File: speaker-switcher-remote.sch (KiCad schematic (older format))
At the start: 17 parts, among them M1 arduino-nano, Q1 TIP31C, Q2 TIP31C

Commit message: Updated with arduino src code
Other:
- moved on the sheet: IR1, M1, OUT+1, OUT-1, PWR+1, PWR-1, Q1, Q2, R1, R2, R3, R4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

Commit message: Updated as per Dan's recommendations
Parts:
- removed Q1: TIP31C, Package_TO_SOT_THT:TO-220-3_Vertical, symbol Device:Q_NPN_BCE
- removed R4, R5: 1k, Resistor_THT:R_Axial_DIN0207_L6.3mm_D2.5mm_P7.62mm_Horizontal, symbol Device:R
- added C1: .33uF, Capacitor_THT:CP_Radial_D10.0mm_P5.00mm, symbol Device:CP
- added C2: .1uF, Capacitor_THT:CP_Radial_D10.0mm_P5.00mm, symbol Device:CP
- added C3: 100uF, Capacitor_THT:CP_Radial_D10.0mm_P5.00mm, symbol Device:CP
- added C4: 100pF, symbol Device:C
- added D1: 1N4148, symbol Device:D
- added Q1: 2N2222, symbol Device:Q_NPN_EBC
- added R10, R8: 100, symbol Device:R
- added R9: 47k, symbol Device:R
- added U1: LM7805_TO220, Package_TO_SOT_THT:TO-220-3_Vertical, symbol Regulator_Linear:LM7805_TO220
- IR1: symbol arduino:VS1838b -> speaker-switcher-remote-rescue:VS1838b-arduino
- M1: symbol arduino:arduino-nano -> speaker-switcher-remote-rescue:arduino-nano-arduino
- OUT+1, OUT-1, PWR+1, PWR-1, SIG+1, SIG-1: symbol arduino:spade-terminal -> speaker-switcher-remote-rescue:spade-terminal-arduino
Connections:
- net +5V: now also C2.1, R10.1, U1.3 (VO)
- net GNDREF: now also C1.2, C2.2, C3.2, C4.2, U1.2 (GND)
- net OUT+: no longer OUT+1.1, R7.1
- net OUT-: no longer OUT-1.1, Q2.2 (C)
- net PWR: now also C1.1, U1.1 (VI)
- net at IR1.1 (OUT), M1.16 (D12): now also R9.1
- net at M1.2 (3.3V): now also R8.2, R9.2; no longer IR1.3 (VCC)
- net at M1.22 (D06), R1.2: now also Q1.1 (E); no longer R6.2
- new net: D1.2 (A), OUT-1.1, Q2.2 (C)
- new net: C3.1, C4.1, IR1.3 (VCC), R8.1
- new net: D1.1 (K), OUT+1.1, R7.1
- new net: Q1.2 (B), R6.2
- new net: Q1.3 (C), R10.2
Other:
- moved on the sheet: IR1, M1, OUT+1, OUT-1, PWR+1, PWR-1, Q2, R1, R2, R3, R6, R7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

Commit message: Updated board
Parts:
- C1, C2, C3: footprint Capacitor_THT:CP_Radial_D10.0mm_P5.00mm -> Capacitor_THT:CP_Radial_D10.0mm_P2.50mm
- C4: footprint (none) -> Capacitor_THT:C_Disc_D6.0mm_W2.5mm_P5.00mm
- D1: footprint (none) -> Diode_THT:D_DO-41_SOD81_P3.81mm_Vertical_KathodeUp
- Q1: footprint (none) -> Package_TO_SOT_THT:TO-92
- R1, R2, R3, R6: footprint Resistor_THT:R_Axial_DIN0207_L6.3mm_D2.5mm_P7.62mm_Horizontal -> Resistor_THT:R_Axial_DIN0207_L6.3mm_D2.5mm_P2.54mm_Vertical
- R10, R8, R9: footprint (none) -> Resistor_THT:R_Axial_DIN0207_L6.3mm_D2.5mm_P2.54mm_Vertical
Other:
- moved on the sheet: Q1, R10, R6, SIG+1, SIG-1
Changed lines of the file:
@@
 F 0 "R2" V 6843 3400 50  0000 C CNN
 F 1 "2.2k" V 6934 3400 50  0000 C CNN
-F 2 "Resistor_THT:R_Axial_DIN0207_L6.3mm_D2.5mm_P7.62mm_Horizontal" V 6980 3400 50  0001 C CNN
+F 2 "Resistor_THT:R_Axial_DIN0207_L6.3mm_D2.5mm_P2.54mm_Vertical" V 6980 3400 50  0001 C CNN
 F 3 "~" H 7050 3400 50  0001 C CNN
 	1    7050 3400
@@
 F 0 "R3" H 7420 3646 50  0000 L CNN
 F 1 "10k" H 7420 3555 50  0000 L CNN
-F 2 "Resistor_THT:R_Axial_DIN0207_L6.3mm_D2.5mm_P7.62mm_Horizontal" V 7280 3600 50  0001 C CNN
+F 2 "Resistor_THT:R_Axial_DIN0207_L6.3mm_D2.5mm_P2.54mm_Vertical" V 7280 3600 50  0001 C CNN
 F 3 "~" H 7350 3600 50  0001 C CNN
 	1    7350 3600
@@
 F 0 "R1" V 6143 4450 50  0000 C CNN
 F 1 "100k" V 6234 4450 50  0000 C CNN
-F 2 "Resistor_THT:R_Axial_DIN0207_L6.3mm_D2.5mm_P7.62mm_Horizontal" V 6280 4450 50  0001 C CNN
+F 2 "Resistor_THT:R_Axial_DIN0207_L6.3mm_D2.5mm_P2.54mm_Vertical" V 6280 4450 50  0001 C CNN
 F 3 "~" H 6350 4450 50  0001 C CNN
 	1    6350 4450
@@
 L power:GNDREF #PWR0106
 U 1 1 600E3B6B
-P 7850 4550
-F 0 "#PWR0106" H 7850 4300 50  0001 C CNN
-F 1 "GNDREF" H 7855 4377 50  0000 C CNN
-F 2 "" H 7850 4550 50  0001 C CNN
-F 3 "" H 7850 4550 50  0001 C CNN
-	1    7850 4550
+P 7600 4550
+F 0 "#PWR0106" H 7600 4300 50  0001 C CNN
+F 1 "GNDREF" H 7605 4377 50  0000 C CNN
+F 2 "" H 7600 4550 50  0001 C CNN
+F 3 "" H 7600 4550 50  0001 C CNN
+	1    7600 4550
 	1    0    0    -1
 $EndComp
@@
 L speaker-switcher-remote-rescue:spade-terminal-arduino SIG-1
 U 1 1 600B1A54
-P 8000 4550
-F 0 "SIG-1" H 8078 4585 50  0000 L CNN
-F 1 "spade-terminal" H 8050 4450 30  0000 L CNN
-F 2 "arduino-nano:SpadeTerminal635" H 7850 4700 50  0001 C CNN
-F 3 "" H 7850 4700 50  0001 C CNN
-	1    8000 4550
+P 7750 4550
+F 0 "SIG-1" H 7828 4585 50  0000 L CNN
+F 1 "spade-terminal" H 7800 4450 30  0000 L CNN
+F 2 "arduino-nano:SpadeTerminal635" H 7600 4700 50  0001 C CNN
+F 3 "" H 7600 4700 50  0001 C CNN
+	1    7750 4550
 	1    0    0    -1
 $EndComp
@@
 L speaker-switcher-remote-rescue:spade-terminal-arduino SIG+1
 U 1 1 600B3081
-P 8000 4450
-F 0 "SIG+1" H 8078 4485 50  0000 L CNN
-F 1 "spade-terminal" H 8100 4550 30  0000 L CNN
-F 2 "arduino-nano:SpadeTerminal635" H 7850 4600 50  0001 C CNN
-F 3 "" H 7850 4600 50  0001 C CNN
-	1    8000 4450
+P 7750 4450
+F 0 "SIG+1" H 7828 4485 50  0000 L CNN
+F 1 "spade-terminal" H 7850 4550 30  0000 L CNN
+F 2 "arduino-nano:SpadeTerminal635" H 7600 4600 50  0001 C CNN
+F 3 "" H 7600 4600 50  0001 C CNN
+	1    7750 4450
 	1    0    0    -1
 $EndComp
@@
 $EndComp
 Wire Wire Line
-	7900 4550 7850 4550
+	7650 4550 7600 4550
 Text Label 8800 2850 0    50   ~ 0
 OUT+
@@
 F 0 "C1" H 3668 5296 50  0000 L CNN
 F 1 ".33uF" H 3668 5205 50  0000 L CNN
-F 2 "Capacitor_THT:CP_Radial_D10.0mm_P5.00mm" H 3588 5100 50  0001 C CNN
+F 2 "Capacitor_THT:CP_Radial_D10.0mm_P2.50mm" H 3588 5100 50  0001 C CNN
 F 3 "~" H 3550 5250 50  0001 C CNN
 	1    3550 5250
@@
 F 0 "C2" H 4768 5296 50  0000 L CNN
 F 1 ".1uF" H 4768 5205 50  0000 L CNN
-F 2 "Capacitor_THT:CP_Radial_D10.0mm_P5.00mm" H 4688 5100 50  0001 C CNN
+F 2 "Capacitor_THT:CP_Radial_D10.0mm_P2.50mm" H 4688 5100 50  0001 C CNN
 F 3 "~" H 4650 5250 50  0001 C CNN
 	1    4650 5250
@@
 F 0 "R9" V 5500 3150 50  0000 C CNN
 F 1 "47k" V 5600 3150 50  0000 C CNN
-F 2 "" V 5430 3150 50  0001 C CNN
+F 2 "Resistor_THT:R_Axial_DIN0207_L6.3mm_D2.5mm_P2.54mm_Vertical" V 5430 3150 50  0001 C CNN
 F 3 "~" H 5500 3150 50  0001 C CNN
 	1    5500 3150
@@
 F 0 "D1" V 8254 2929 50  0000 L CNN
 F 1 "1N4148" H 8150 2750 50  0000 L CNN
-F 2 "" H 8300 2850 50  0001 C CNN
+F 2 "Diode_THT:D_DO-41_SOD81_P3.81mm_Vertical_KathodeUp" H 8300 2850 50  0001 C CNN
 F 3 "~" H 8300 2850 50  0001 C CNN
 	1    8300 2850
@@
 L Device:Q_NPN_EBC Q1
 U 1 1 602A1BF3
-P 7400 4450
-F 0 "Q1" H 7591 4404 50  0000 L CNN
-F 1 "2N2222" H 7591 4495 50  0000 L CNN
-F 2 "" H 7600 4550 50  0001 C CNN
-F 3 "~" H 7400 4450 50  0001 C CNN
-	1    7400 4450
+P 7150 4450
+F 0 "Q1" V 7450 4400 50  0000 L CNN
+F 1 "2N2222" V 7350 4300 50  0000 L CNN
+F 2 "Package_TO_SOT_THT:TO-92" H 7350 4550 50  0001 C CNN
+F 3 "~" H 7150 4450 50  0001 C CNN
+	1    7150 4450
 	-1   0    0    1
 $EndComp
 Wire Wire Line
-	6350 4150 7300 4150
-Text GLabel 7300 5100 3    50   Input ~ 0
+	6350 4150 7050 4150
+Text GLabel 7050 5100 3    50   Input ~ 0
 +5V
 Wire Wire Line
-	7300 4150 7300 4250
-Wire Wire Line
-	7300 4650 7300 4700
+	7050 4150 7050 4250
+Wire Wire Line
+	7050 4650 7050 4700
 Wire Wire Line
 	6300 2150 6250 2150
@@
 F 0 "R8" H 5020 2646 50  0000 L CNN
 F 1 "100" H 5020 2555 50  0000 L CNN
-F 2 "" V 4880 2600 50  0001 C CNN
+F 2 "Resistor_THT:R_Axial_DIN0207_L6.3mm_D2.5mm_P2.54mm_Vertical" V 4880 2600 50  0001 C CNN
 F 3 "~" H 4950 2600 50  0001 C CNN
 	1    4950 2600
@@
 L Device:R R6
 U 1 1 600BEA2A
-P 7750 4450
-F 0 "R6" V 7543 4450 50  0000 C CNN
-F 1 "2.2k" V 7634 4450 50  0000 C CNN
-F 2 "Resistor_THT:R_Axial_DIN0207_L6.3mm_D2.5mm_P7.62mm_Horizontal" V 7680 4450 50  0001 C CNN
-F 3 "~" H 7750 4450 50  0001 C CNN
-	1    7750 4450
+P 7500 4450
+F 0 "R6" V 7293 4450 50  0000 C CNN
+F 1 "2.2k" V 7384 4450 50  0000 C CNN
+F 2 "Resistor_THT:R_Axial_DIN0207_L6.3mm_D2.5mm_P2.54mm_Vertical" V 7430 4450 50  0001 C CNN
+F 3 "~" H 7500 4450 50  0001 C CNN
+	1    7500 4450
 	0    1    1    0
 $EndComp
@@
 F 0 "C3" H 5600 2450 50  0000 L CNN
 F 1 "100uF" H 5600 2250 50  0000 L CNN
-F 2 "Capacitor_THT:CP_Radial_D10.0mm_P5.00mm" H 5638 2200 50  0001 C CNN
+F 2 "Capacitor_THT:CP_Radial_D10.0mm_P2.50mm" H 5638 2200 50  0001 C CNN
 F 3 "~" H 5600 2350 50  0001 C CNN
 	1    5600 2350
@@
 F 0 "C4" H 5300 2450 50  0000 L CNN
 F 1 "100pF" H 5300 2250 50  0000 L CNN
-F 2 "" H 5338 2200 50  0001 C CNN
+F 2 "Capacitor_THT:C_Disc_D6.0mm_W2.5mm_P5.00mm" H 5338 2200 50  0001 C CNN
 F 3 "~" H 5300 2350 50  0001 C CNN
 	1    5300 2350
@@
 L Device:R R10
 U 1 1 603B8358
-P 7300 4850
-F 0 "R10" H 7230 4804 50  0000 R CNN
-F 1 "100" H 7230 4895 50  0000 R CNN
-F 2 "" V 7230 4850 50  0001 C CNN
-F 3 "~" H 7300 4850 50  0001 C CNN
-	1    7300 4850
+P 7050 4850
+F 0 "R10" H 6980 4804 50  0000 R CNN
+F 1 "100" H 6980 4895 50  0000 R CNN
+F 2 "Resistor_THT:R_Axial_DIN0207_L6.3mm_D2.5mm_P2.54mm_Vertical" V 6980 4850 50  0001 C CNN
+F 3 "~" H 7050 4850 50  0001 C CNN
+	1    7050 4850
 	-1   0    0    1
 $EndComp
 Wire Wire Line
-	7300 5000 7300 5100
+	7050 5000 7050 5100
 $EndSCHEMATC

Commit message: New PCB layout
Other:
- moved on the sheet: R9
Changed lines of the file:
@@
 	6050 3550 6300 3550
 Wire Wire Line
-	6300 2150 6300 3150
-Connection ~ 6300 3150
+	6300 2150 6300 3050
+Connection ~ 6300 3050
 Wire Wire Line
-	6300 3150 6300 3550
+	6300 3050 6300 3550
 $Comp
 L Device:R R9
 U 1 1 601BDAF6
-P 5500 3150
-F 0 "R9" V 5500 3150 50  0000 C CNN
-F 1 "47k" V 5600 3150 50  0000 C CNN
-F 2 "Resistor_THT:R_Axial_DIN0207_L6.3mm_D2.5mm_P2.54mm_Vertical" V 5430 3150 50  0001 C CNN
-F 3 "~" H 5500 3150 50  0001 C CNN
-	1    5500 3150
+P 5500 3050
+F 0 "R9" V 5500 3050 50  0000 C CNN
+F 1 "47k" V 5600 3050 50  0000 C CNN
+F 2 "Resistor_THT:R_Axial_DIN0207_L6.3mm_D2.5mm_P2.54mm_Vertical" V 5430 3050 50  0001 C CNN
+F 3 "~" H 5500 3050 50  0001 C CNN
+	1    5500 3050
 	0    1    1    0
 $EndComp
 Wire Wire Line
-	5650 3150 6300 3150
+	5650 3050 6300 3050
 Wire Wire Line
 	7200 3400 7350 3400
@@
 	6300 2150 6250 2150
 Wire Wire Line
-	4950 3150 4950 2750
-Connection ~ 4950 3150
+	4950 3050 4950 2750
+Connection ~ 4950 3050
 Wire Wire Line
-	4950 3150 5350 3150
+	4950 3050 5350 3050
 Wire Wire Line
 	4950 2150 4950 2450
@@
 	4950 3650 5150 3650
 Wire Wire Line
-	4950 3650 4950 3150
+	4950 3650 4950 3050
 Wire Wire Line
 	4650 4950 5150 4950

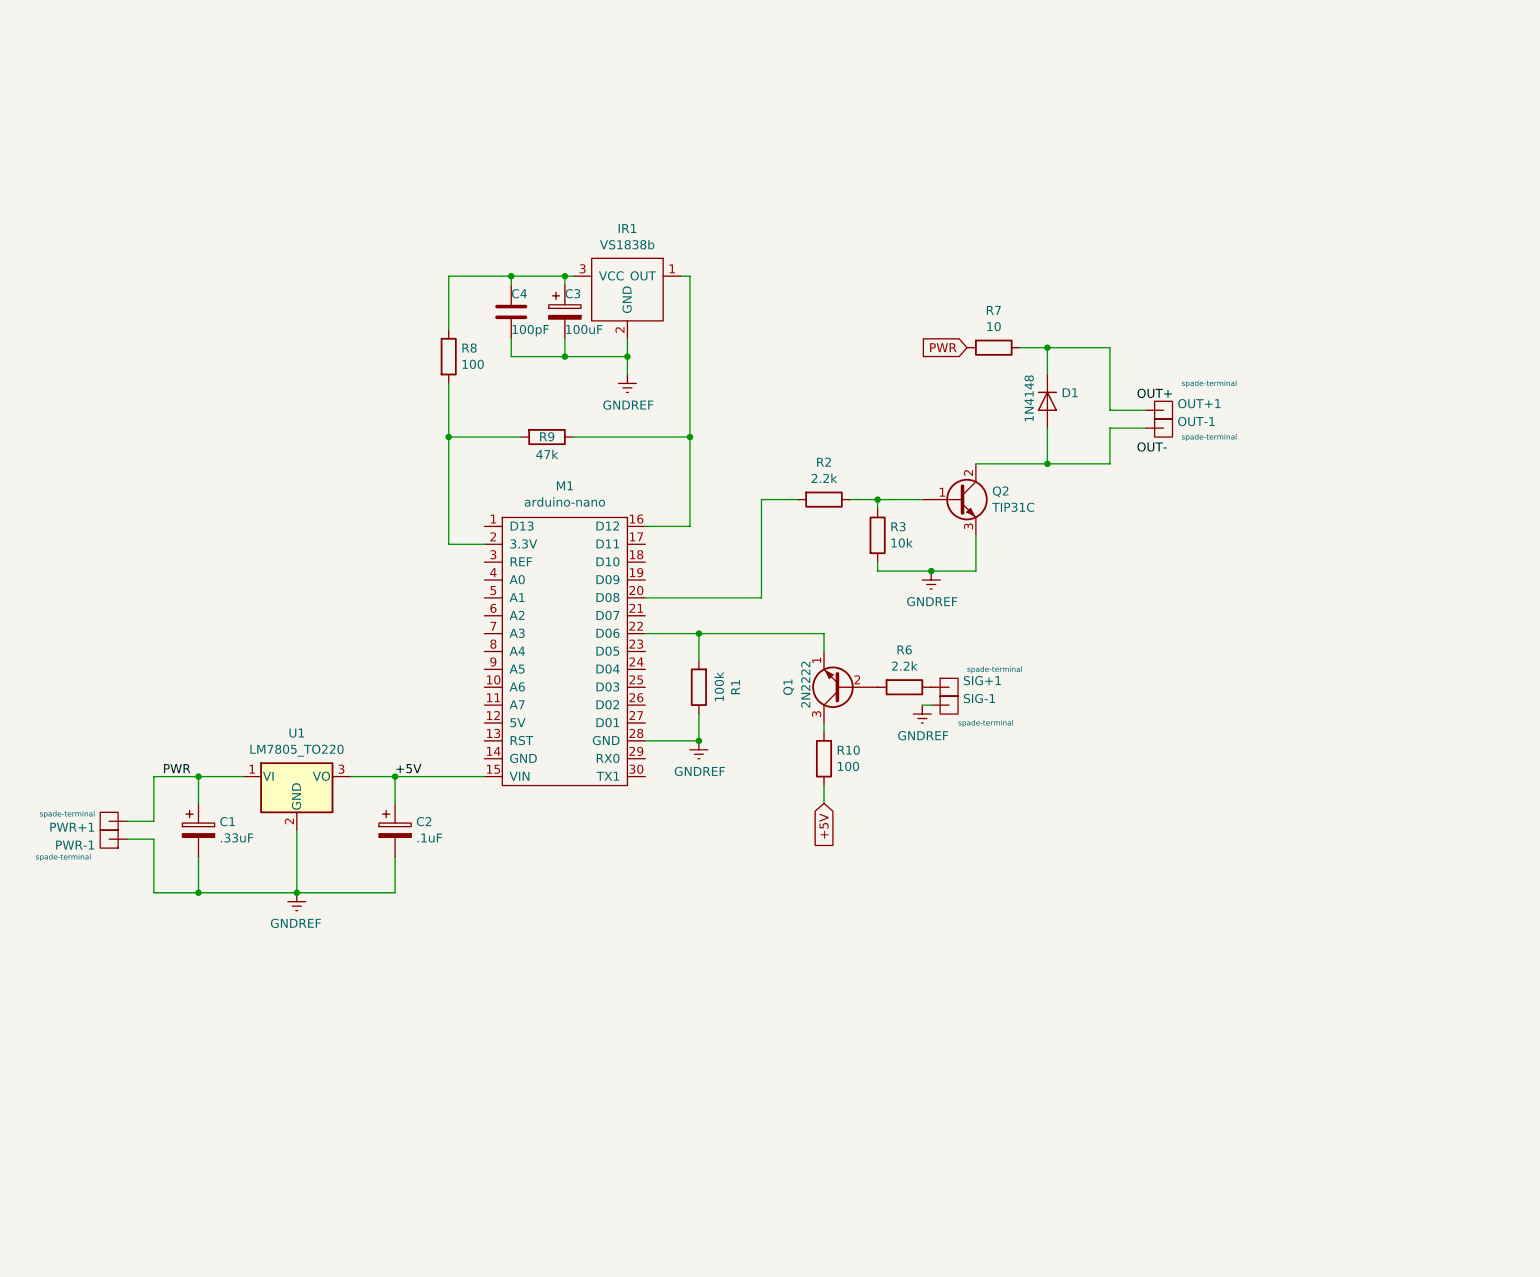
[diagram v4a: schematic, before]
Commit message: Stabilize signal input
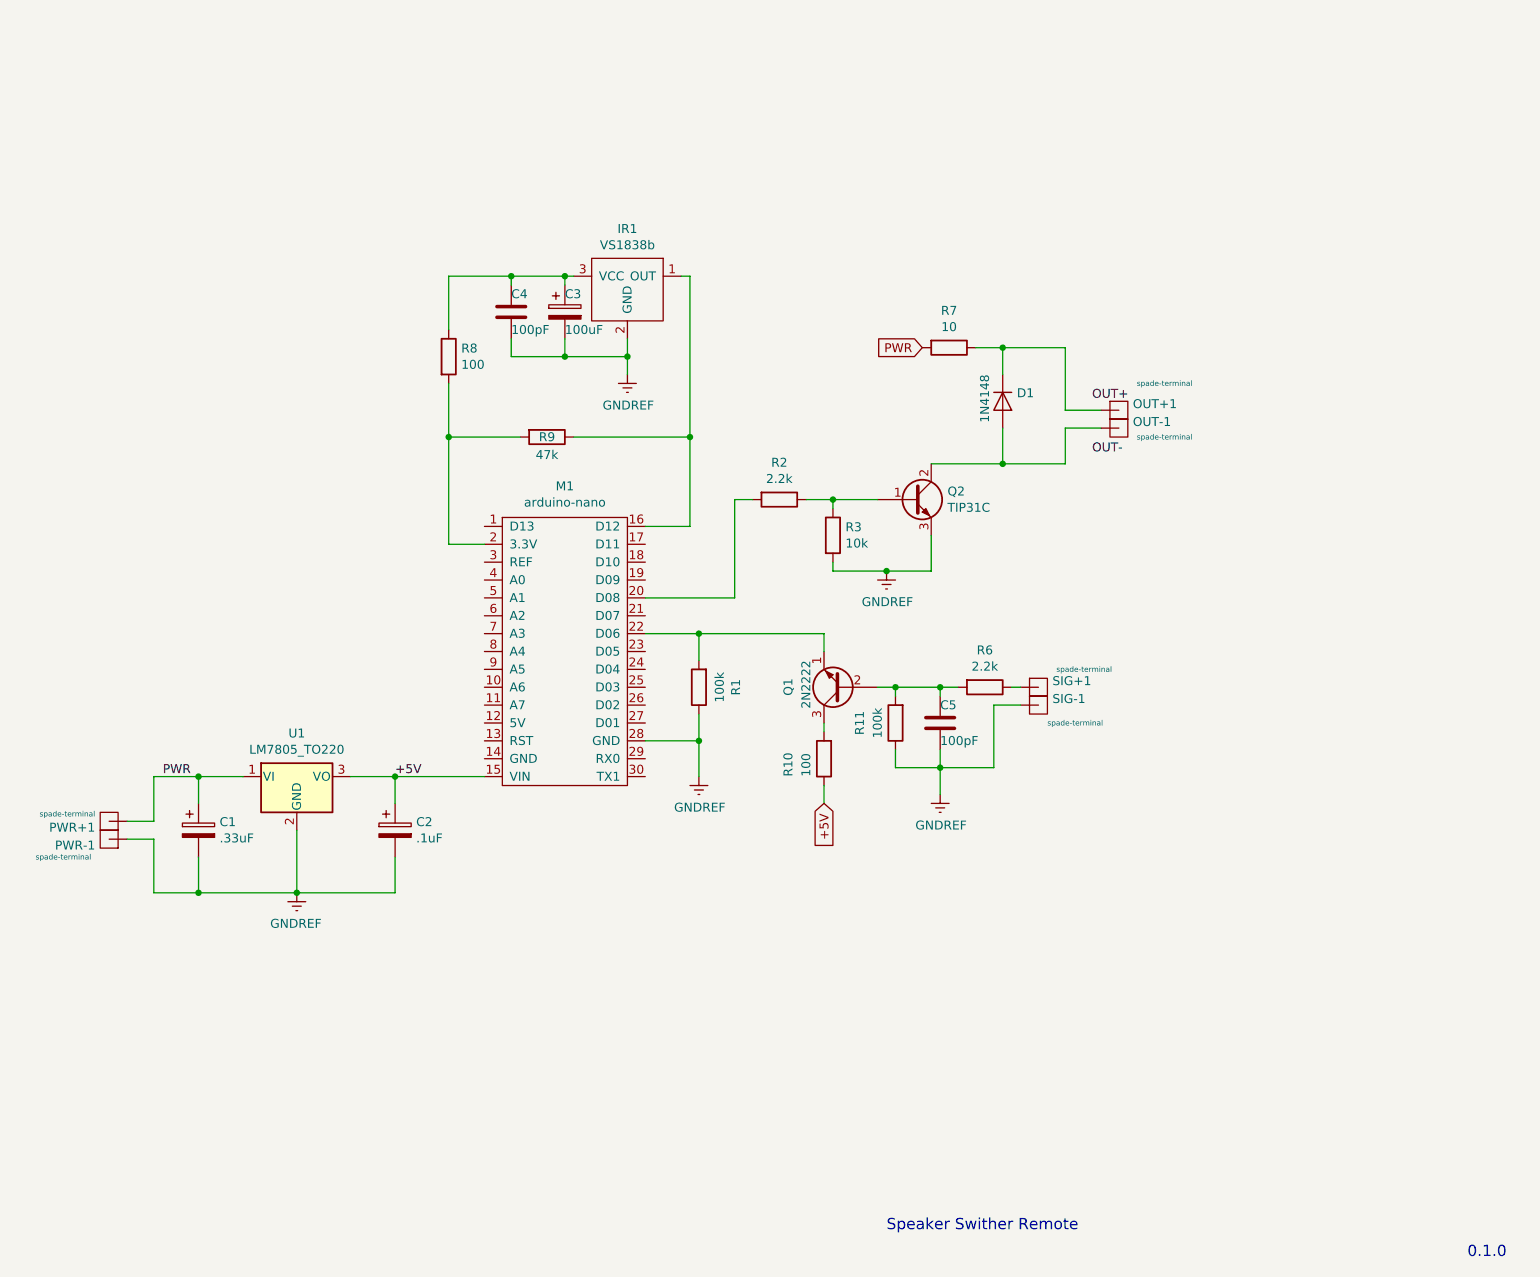
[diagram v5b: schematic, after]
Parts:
- added C5: 100pF, Capacitor_THT:C_Disc_D6.0mm_W2.5mm_P5.00mm, symbol Device:C
- added R11: 100k, Resistor_THT:R_Axial_DIN0207_L6.3mm_D2.5mm_P2.54mm_Vertical, symbol Device:R
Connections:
- net GNDREF: now also C5.2, R11.1
- net at Q1.2 (B), R6.2: now also C5.1, R11.2
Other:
- note added: "0.1.0"
- note added: "Speaker Swither Remote"
- moved on the sheet: D1, OUT+1, OUT-1, Q2, R2, R3, R6, R7, SIG+1, SIG-1

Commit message: Updated PCB but not plots
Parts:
- D1: footprint Diode_THT:D_DO-41_SOD81_P3.81mm_Vertical_KathodeUp -> Diode_THT:D_DO-41_SOD81_P7.62mm_Horizontal
- R1, R10, R11, R2, R3, R6, R8, R9: footprint Resistor_THT:R_Axial_DIN0207_L6.3mm_D2.5mm_P2.54mm_Vertical -> Resistor_THT:R_Axial_DIN0207_L6.3mm_D2.5mm_P7.62mm_Horizontal
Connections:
- net at IR1.1 (OUT), M1.16 (D12): now also R9.2; no longer R9.1
- net at M1.2 (3.3V), R8.2: now also R9.1; no longer R9.2
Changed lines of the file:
@@
 F 0 "R2" V 6593 3400 50  0000 C CNN
 F 1 "2.2k" V 6684 3400 50  0000 C CNN
-F 2 "Resistor_THT:R_Axial_DIN0207_L6.3mm_D2.5mm_P2.54mm_Vertical" V 6730 3400 50  0001 C CNN
+F 2 "Resistor_THT:R_Axial_DIN0207_L6.3mm_D2.5mm_P7.62mm_Horizontal" V 6730 3400 50  0001 C CNN
 F 3 "~" H 6800 3400 50  0001 C CNN
 	1    6800 3400
@@
 F 0 "R1" V 6143 4450 50  0000 C CNN
 F 1 "100k" V 6234 4450 50  0000 C CNN
-F 2 "Resistor_THT:R_Axial_DIN0207_L6.3mm_D2.5mm_P2.54mm_Vertical" V 6280 4450 50  0001 C CNN
+F 2 "Resistor_THT:R_Axial_DIN0207_L6.3mm_D2.5mm_P7.62mm_Horizontal" V 6280 4450 50  0001 C CNN
 F 3 "~" H 6350 4450 50  0001 C CNN
 	1    6350 4450
@@
 Wire Wire Line
 	6300 3050 6300 3550
-$Comp
-L Device:R R9
-U 1 1 601BDAF6
-P 5500 3050
-F 0 "R9" V 5500 3050 50  0000 C CNN
-F 1 "47k" V 5600 3050 50  0000 C CNN
-F 2 "Resistor_THT:R_Axial_DIN0207_L6.3mm_D2.5mm_P2.54mm_Vertical" V 5430 3050 50  0001 C CNN
-F 3 "~" H 5500 3050 50  0001 C CNN
-	1    5500 3050
-	0    1    1    0
-$EndComp
 Wire Wire Line
 	5650 3050 6300 3050
@@
 F 0 "D1" V 8004 2929 50  0000 L CNN
 F 1 "1N4148" H 7900 2750 50  0000 L CNN
-F 2 "Diode_THT:D_DO-41_SOD81_P3.81mm_Vertical_KathodeUp" H 8050 2850 50  0001 C CNN
+F 2 "Diode_THT:D_DO-41_SOD81_P7.62mm_Horizontal" H 8050 2850 50  0001 C CNN
 F 3 "~" H 8050 2850 50  0001 C CNN
 	1    8050 2850
@@
 F 0 "R8" H 5020 2646 50  0000 L CNN
 F 1 "100" H 5020 2555 50  0000 L CNN
-F 2 "Resistor_THT:R_Axial_DIN0207_L6.3mm_D2.5mm_P2.54mm_Vertical" V 4880 2600 50  0001 C CNN
+F 2 "Resistor_THT:R_Axial_DIN0207_L6.3mm_D2.5mm_P7.62mm_Horizontal" V 4880 2600 50  0001 C CNN
 F 3 "~" H 4950 2600 50  0001 C CNN
 	1    4950 2600
@@
 F 0 "R6" V 7743 4450 50  0000 C CNN
 F 1 "2.2k" V 7834 4450 50  0000 C CNN
-F 2 "Resistor_THT:R_Axial_DIN0207_L6.3mm_D2.5mm_P2.54mm_Vertical" V 7880 4450 50  0001 C CNN
+F 2 "Resistor_THT:R_Axial_DIN0207_L6.3mm_D2.5mm_P7.62mm_Horizontal" V 7880 4450 50  0001 C CNN
 F 3 "~" H 7950 4450 50  0001 C CNN
 	1    7950 4450
@@
 F 0 "R10" V 7250 4950 50  0000 R CNN
 F 1 "100" V 7150 4950 50  0000 R CNN
-F 2 "Resistor_THT:R_Axial_DIN0207_L6.3mm_D2.5mm_P2.54mm_Vertical" V 6980 4850 50  0001 C CNN
+F 2 "Resistor_THT:R_Axial_DIN0207_L6.3mm_D2.5mm_P7.62mm_Horizontal" V 6980 4850 50  0001 C CNN
 F 3 "~" H 7050 4850 50  0001 C CNN
 	1    7050 4850
@@
 F 0 "R11" V 7650 4650 50  0000 C CNN
 F 1 "100k" V 7550 4650 50  0000 C CNN
-F 2 "Resistor_THT:R_Axial_DIN0207_L6.3mm_D2.5mm_P2.54mm_Vertical" V 7380 4650 50  0001 C CNN
+F 2 "Resistor_THT:R_Axial_DIN0207_L6.3mm_D2.5mm_P7.62mm_Horizontal" V 7380 4650 50  0001 C CNN
 F 3 "~" H 7450 4650 50  0001 C CNN
 	1    7450 4650
@@
 F 0 "R3" H 7170 3646 50  0000 L CNN
 F 1 "10k" H 7170 3555 50  0000 L CNN
-F 2 "Resistor_THT:R_Axial_DIN0207_L6.3mm_D2.5mm_P2.54mm_Vertical" V 7030 3600 50  0001 C CNN
+F 2 "Resistor_THT:R_Axial_DIN0207_L6.3mm_D2.5mm_P7.62mm_Horizontal" V 7030 3600 50  0001 C CNN
 F 3 "~" H 7100 3600 50  0001 C CNN
 	1    7100 3600
@@
 Wire Wire Line
 	6350 4750 6350 4950
+$Comp
+L Device:R R9
+U 1 1 601BDAF6
+P 5500 3050
+F 0 "R9" V 5500 3050 50  0000 C CNN
+F 1 "47k" V 5600 3050 50  0000 C CNN
+F 2 "Resistor_THT:R_Axial_DIN0207_L6.3mm_D2.5mm_P7.62mm_Horizontal" V 5430 3050 50  0001 C CNN
+F 3 "~" H 5500 3050 50  0001 C CNN
+	1    5500 3050
+	0    -1   -1   0
+$EndComp
 $EndSCHEMATC
